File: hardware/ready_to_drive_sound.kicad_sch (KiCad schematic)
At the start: 6 parts, among them Q10 NMOS

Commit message: Add the Cube project
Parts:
- removed C?: 100n, Capacitor_SMD:C_0603_1608Metric, symbol Device:C_Small
- removed Q10: NMOS, symbol Simulation_SPICE:NMOS
- removed U?: MCP14A0052T, Package_TO_SOT_SMD:SOT-23-6, symbol Traction_Control_System-rescue:MCP14A0052T-PUTM_KICAD_SYMBOLS
- added Q5: PMV450ENEA, symbol Simulation_SPICE:NMOS
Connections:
- net GND: now also Q5.3 (S)
- net IN: now also R?.2
- net at R?.1: now also Q5.1 (D)
- net at R?.1, R?.2: now also Q5.2 (G)
- no-connect marks 1 -> 0
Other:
- note removed: "TODO: change to 3v3 compatibile driver"
- moved on the sheet: R?

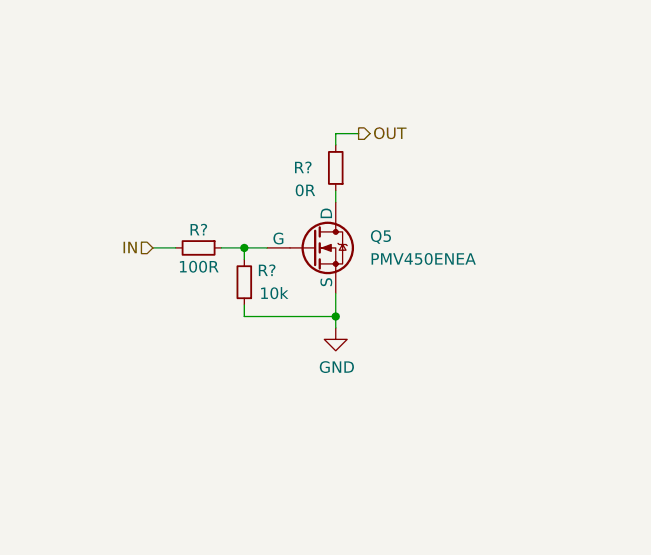
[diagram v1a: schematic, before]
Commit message: Improve the schematic
- add anti-aliasing filters
- rearrange the main connector signals
- improve the power filtering
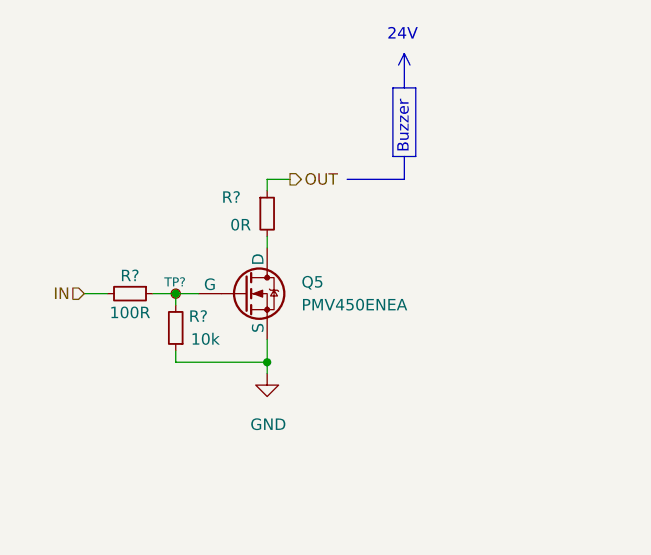
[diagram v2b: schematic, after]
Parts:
- removed R?: 0R, Resistor_SMD:R_0603_1608Metric, symbol Device:R_Small
- added R?: 0R, Resistor_SMD:R_0603_1608Metric, symbol Device:R_Small
- added TP?: TestPoint_Small, TestPoint:TestPoint_Pad_D1.0mm, symbol Connector:TestPoint_Small
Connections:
- net OUT: now also R?.1
- net at Q5.1 (D): now also R?.2
- net at Q5.2 (G), R?.1, R?.2: now also TP?.1
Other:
- note added: "24V"
- note added: "Buzzer"
- moved on the sheet: Q5, R?

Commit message: Set component values
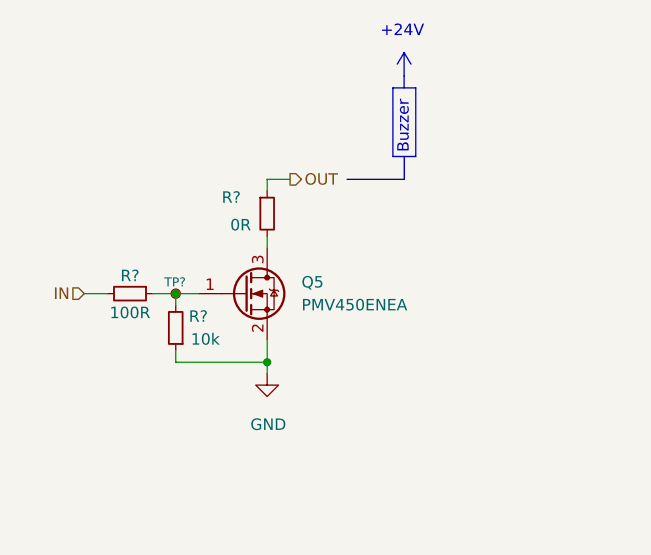
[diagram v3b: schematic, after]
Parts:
- Q5: symbol Simulation_SPICE:NMOS -> Device:Q_NMOS_GSD
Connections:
- net GND: now also Q5.2 (S); no longer Q5.3 (S)
- net at Q5.1 (G): now also R?.1, R?.2, TP?.1; no longer R?.2
- new net: Q5.3 (D), R?.2
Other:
- note added: "+24V"
- note removed: "24V"
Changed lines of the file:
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@@
-    (stroke (width 0) (type default))
-  )
-  (polyline (pts (xy 160.655 81.28) (xy 161.29 80.01))
     (stroke (width 0) (type default))
   )
@@
     (stroke (width 0) (type default))
   )
+  (polyline (pts (xy 161.2646 79.9084) (xy 161.2646 82.4738))
+    (stroke (width 0) (type default))
+  )
   (polyline (pts (xy 161.29 91.44) (xy 161.29 93.98))
     (stroke (width 0) (type default))
@@
     (stroke (width 0) (type default))
   )
+  (polyline (pts (xy 160.5026 81.1784) (xy 161.2646 79.9084))
+    (stroke (width 0) (type default))
+  )
   (polyline (pts (xy 160.02 91.44) (xy 160.02 83.82))
     (stroke (width 0) (type default))
@@
     (stroke (width 0) (type default))
   )
-  (polyline (pts (xy 161.29 80.01) (xy 161.29 83.82))
+  (polyline (pts (xy 161.2646 82.5246) (xy 161.2646 83.7946))
     (stroke (width 0) (type default))
   )
@@
     (stroke (width 0) (type default))
   )
-  (polyline (pts (xy 161.29 80.01) (xy 161.925 81.28))
-    (stroke (width 0) (type default))
-  )
-  (text "24V" (at 159.385 78.74 0)
+  (polyline (pts (xy 162.0266 81.1784) (xy 161.2646 79.9084))
+    (stroke (width 0) (type default))
+  )
+  (text "+24V" (at 158.623 78.359 0)
     (effects (font (size 1.27 1.27)) (justify left bottom))
   )
@@
     (effects (font (size 1.27 1.27)) (justify left))
   )
-  (symbol (lib_id "Simulation_SPICE:NMOS") (at 143.51 106.68 0) (unit 1)
+  (symbol (lib_id "Device:Q_NMOS_GSD") (at 143.51 106.68 0) (unit 1)
     (in_bom yes) (on_board yes) (dnp no)
     (property "Reference" "Q5" (at 149.86 105.41 0)
@@
       (effects (font (size 1.27 1.27)) hide)
     )
-    (property "Datasheet" "https://assets.nexperia.com/documents/data-sheet/PMV450ENEA.pdf" (at 143.51 119.38 0)
+    (property "Datasheet" "~" (at 143.51 106.68 0)
       (effects (font (size 1.27 1.27)) hide)
     )
@@
         )
         (path "/b652b05a-4e3d-4ad1-b032-18886abe7d45/562e38ba-d94a-4627-8fa0-e9eb7b5e4e9a"
-          (reference "R108") (unit 1)
+          (reference "R110") (unit 1)
         )
         (path "/b652b05a-4e3d-4ad1-b032-18886abe7d45/6999686b-4026-4ea7-9227-634603a79198"
@@
         )
         (path "/b652b05a-4e3d-4ad1-b032-18886abe7d45/562e38ba-d94a-4627-8fa0-e9eb7b5e4e9a"
-          (reference "R107") (unit 1)
+          (reference "R109") (unit 1)
         )
         (path "/b652b05a-4e3d-4ad1-b032-18886abe7d45/6999686b-4026-4ea7-9227-634603a79198"
@@
         )
         (path "/b652b05a-4e3d-4ad1-b032-18886abe7d45/562e38ba-d94a-4627-8fa0-e9eb7b5e4e9a"
-          (reference "R106") (unit 1)
+          (reference "R108") (unit 1)
         )
         (path "/b652b05a-4e3d-4ad1-b032-18886abe7d45/6999686b-4026-4ea7-9227-634603a79198"

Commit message: Improve the schematic according to the feedback
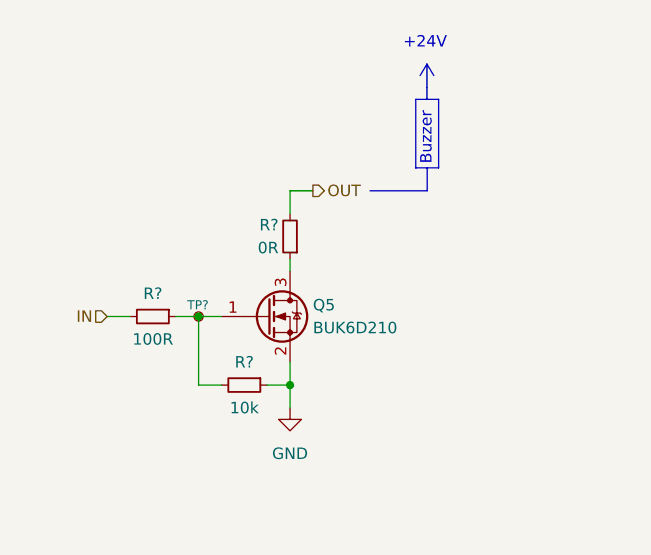
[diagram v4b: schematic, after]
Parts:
- removed R?: 0R, Resistor_SMD:R_0603_1608Metric, symbol Device:R_Small
- removed R?: 10k, Resistor_SMD:R_0603_1608Metric, symbol Device:R_Small
- removed R?: 100R, Resistor_SMD:R_0603_1608Metric, symbol Device:R_Small
- removed TP?: TestPoint_Small, TestPoint:TestPoint_Pad_D1.0mm, symbol Connector:TestPoint_Small
- added R?: 10k, Resistor_SMD:R_0603_1608Metric, symbol Device:R_Small
- added R?: 100R, Resistor_SMD:R_0603_1608Metric, symbol Device:R_Small
- added R?: 0R, Resistor_SMD:R_0603_1608Metric, symbol Device:R_Small
- added TP?: TestPoint_Small, TestPoint:TestPoint_Pad_D1.0mm, symbol Connector:TestPoint_Small
- Q5: value PMV450ENEA -> BUK6D210; footprint (none) -> Package_DFN_QFN:Diodes_UDFN2020-6_Type-F
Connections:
- net GND: now also R?.1
- net IN: now also R?.2
- net OUT: now also R?.2
- net at Q5.1 (G): now also R?.1, R?.2, TP?.1
- net at Q5.3 (D): now also R?.1
